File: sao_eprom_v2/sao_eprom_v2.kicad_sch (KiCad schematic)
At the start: 8 parts, among them J1 USB_C_Receptacle_USB2.0, J2 Conn_01x03, U1 RP2040, X1 YSO110TR

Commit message: More works on eprom v2
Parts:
- removed U?: 74LS161, symbol 74xx:74LS161
- removed U?: 27C512, Package_DIP:DIP-28_W15.24mm, symbol Memory_EPROM:27C512
- added C1, C2, C3, C4: 100n, Capacitor_SMD:C_0402_1005Metric, symbol Device:C_Small
- added J3: Conn_02x03_Odd_Even, Connector_PinHeader_2.54mm:PinHeader_2x03_P2.54mm_Vertical, symbol Connector_Generic:Conn_02x03_Odd_Even
- added R1, R2, R3, R4, R5: 10K, Resistor_SMD:R_0402_1005Metric_Pad0.72x0.64mm_HandSolder, symbol Device:R
- added R8, R9: 27R, Resistor_SMD:R_0402_1005Metric_Pad0.72x0.64mm_HandSolder, symbol Device:R
- added U1: W25Q128JVS, Package_SO:SOIC-8_5.23x5.23mm_P1.27mm, symbol Memory_Flash:W25Q128JVS
- added U3: 24LC00, Package_SO:SOIC-8_3.9x4.9mm_P1.27mm, symbol Memory_EEPROM:24LC00
- J2: renamed from J1; footprint (none) -> Connector_USB:USB_C_Receptacle_G-Switch_GT-USB-7010ASV
- R6: renamed from R1; footprint Resistor_THT:R_Axial_DIN0207_L6.3mm_D2.5mm_P10.16mm_Horizontal -> Resistor_SMD:R_0402_1005Metric_Pad0.72x0.64mm_HandSolder
- R7: renamed from R2; footprint Resistor_THT:R_Axial_DIN0207_L6.3mm_D2.5mm_P10.16mm_Horizontal -> Resistor_SMD:R_0402_1005Metric_Pad0.72x0.64mm_HandSolder
- renumbered J2 to J1, U1 to U2
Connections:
- net +3V3: now also C1.2, C2.2, C3.2, C4.2, J3.2 (Pin_2), U1.8 (VCC), U3.8 (VCC)
- net GND: now also C1.1, C2.1, C3.1, C4.1, J3.1 (Pin_1), R1.2, R2.2, R3.2, R4.2, R5.2, U1.4 (GND), U3.1 (A0), U3.2 (A1), U3.3 (A2), U3.4 (GND), U3.7 (WP)
- net USB_DM: now also R8.2; no longer J2.A7 (D-), J2.B7 (D-)
- net USB_DP: now also R9.2; no longer J2.A6 (D+), J2.B6 (D+)
- net SBU1: now reaches J2.A8 (SBU1)
- net SBU1: now also J2.B8 (SBU2)
- net EPROM and level shifters/D0: now reaches U2.11 (GPIO8)
- net EPROM and level shifters/D1: now reaches U2.12 (GPIO9)
- net EPROM and level shifters/D2: now reaches U2.13 (GPIO10)
- net EPROM and level shifters/D3: now reaches U2.14 (GPIO11)
- net EPROM and level shifters/D4: now reaches U2.15 (GPIO12)
- net EPROM and level shifters/D5: now reaches U2.16 (GPIO13)
- net EPROM and level shifters/D6: now reaches U2.17 (GPIO14)
- net EPROM and level shifters/D7: now reaches U2.18 (GPIO15)
- net EPROM and level shifters/A0: now reaches U2.2 (GPIO0)
- net EPROM and level shifters/OE: now reaches U2.27 (GPIO16)
- net EPROM and level shifters/~{OE}: now reaches U2.28 (GPIO17)
- net EPROM and level shifters/ALS: now reaches U2.29 (GPIO18)
- net EPROM and level shifters/A1: now reaches U2.3 (GPIO1)
- net EPROM and level shifters/AHS: now reaches U2.30 (GPIO19)
- net SDA: now reaches U2.31 (GPIO20)
- net SDA: now also J3.4 (Pin_4), U3.5 (SDA)
- net SCL: now reaches U2.32 (GPIO21)
- net SCL: now also J3.3 (Pin_3), U3.6 (SCL)
- net Power generation/5VEN: now reaches U2.34 (GPIO22)
- net Power generation/5VEN: now also R1.1
- net Power generation/12V75EN: now reaches U2.35 (GPIO23)
- net Power generation/12V75EN: now also R2.1
- net Power generation/VppAEN: now reaches U2.36 (GPIO24)
- net Power generation/VppAEN: now also R3.1
- net Power generation/VppBEN: now reaches U2.37 (GPIO25)
- net Power generation/VppBEN: now also R4.1
- net Power generation/VdetEN: now reaches U2.38 (GPIO26_ADC0)
- net Power generation/VdetEN: now also R5.1
- net EPROM and level shifters/A2: now reaches U2.4 (GPIO2)
- net EPROM and level shifters/A3: now reaches U2.5 (GPIO3)
- net at U2.51 (QSPI_SD3): now also U1.7 (IO3)
- net at U2.52 (QSPI_SCLK): now also U1.6 (CLK)
- net at U2.53 (QSPI_SD0): now also U1.5 (DI(IO0))
- net at U2.54 (QSPI_SD2): now also U1.3 (IO2)
- net at U2.55 (QSPI_SD1): now also U1.2 (DO(IO1))
- net at U2.56 (QSPI_SS): now also U1.1 (~{CS})
- net EPROM and level shifters/A4: now reaches U2.6 (GPIO4)
- net EPROM and level shifters/A5: now reaches U2.7 (GPIO5)
- net EPROM and level shifters/A6: now reaches U2.8 (GPIO6)
- net EPROM and level shifters/A7: now reaches U2.9 (GPIO7)
- new net: J2.A6 (D+), J2.B6 (D+), R9.1
- new net: J2.A7 (D-), J2.B7 (D-), R8.1
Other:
- added sheet EPROM and level shifters (eprom.kicad_sch)
- added sheet Power generation (power.kicad_sch)
- note added: "Logic level 3.3V"
- moved on the sheet: J1, J2, R6, R7, U2, X1

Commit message: the experiment
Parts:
- removed J3: Conn_02x03_Odd_Even, Connector_PinHeader_2.54mm:PinHeader_2x03_P2.54mm_Vertical, symbol Connector_Generic:Conn_02x03_Odd_Even
- added C14, C15, C16, C17, C18, C19, C20, C21, C22: 100n, Capacitor_SMD:C_0402_1005Metric_Pad0.74x0.62mm_HandSolder, symbol Device:C_Small
- added J3: sao_v2_addon_tht, simple_add_on_v2:sao_v2_addon_tht, symbol simple_add_on_v2:sao_v2_addon_tht
- C1, C2, C3, C4: footprint Capacitor_SMD:C_0402_1005Metric -> Capacitor_SMD:C_0402_1005Metric_Pad0.74x0.62mm_HandSolder
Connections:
- net +3V3: now also C14.1, C15.1, C16.2, C17.2, C18.2, C19.2, C20.2, J3.1 (3V3)
- net GND: now also C14.2, C15.2, C16.1, C17.1, C18.1, C19.1, C20.1, C21.1, C22.1, J3.2 (GND)
- net SBU1: now also U2.40 (GPIO28_ADC2); no longer J2.B8 (SBU2)
- net SCL: now also J3.4 (SCL)
- net SDA: now also J3.3 (SDA)
- net +1V1: now reaches U2.23 (DVDD), U2.45 (VREG_VOUT), U2.50 (DVDD)
- net +1V1: now also C21.2, C22.2
- net SBU2: now reaches U2.41 (GPIO29_ADC3)
- net SBU2: now also J2.B8 (SBU2)
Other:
- moved on the sheet: C1, C2, C3, C4

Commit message: More tricky routing.
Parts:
- added C23: 100n, Capacitor_SMD:C_0402_1005Metric_Pad0.74x0.62mm_HandSolder, symbol Device:C_Small
- added H1, H2, H3, H4: MountingHole_Pad, MountingHole:MountingHole_2.2mm_M2_Pad_Via, symbol Mechanical:MountingHole_Pad
- X1: value YSO110TR -> SX3M12.000M20F30TNN
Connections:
- net +3V3: now also C23.1
- net EPROM and level shifters/A0: now also U2.11 (GPIO8); no longer U2.2 (GPIO0)
- net EPROM and level shifters/A1: now also U2.12 (GPIO9); no longer U2.3 (GPIO1)
- net EPROM and level shifters/A2: now also U2.13 (GPIO10); no longer U2.4 (GPIO2)
- net EPROM and level shifters/A3: now also U2.14 (GPIO11); no longer U2.5 (GPIO3)
- net EPROM and level shifters/A4: now also U2.15 (GPIO12); no longer U2.6 (GPIO4)
- net EPROM and level shifters/A5: now also U2.16 (GPIO13); no longer U2.7 (GPIO5)
- net EPROM and level shifters/A6: now also U2.17 (GPIO14); no longer U2.8 (GPIO6)
- net EPROM and level shifters/A7: now also U2.18 (GPIO15); no longer U2.9 (GPIO7)
- net EPROM and level shifters/D0: now also U2.2 (GPIO0); no longer U2.11 (GPIO8)
- net EPROM and level shifters/D1: now also U2.3 (GPIO1); no longer U2.12 (GPIO9)
- net EPROM and level shifters/D2: now also U2.4 (GPIO2); no longer U2.13 (GPIO10)
- net EPROM and level shifters/D3: now also U2.5 (GPIO3); no longer U2.14 (GPIO11)
- net EPROM and level shifters/D4: now also U2.6 (GPIO4); no longer U2.15 (GPIO12)
- net EPROM and level shifters/D5: now also U2.7 (GPIO5); no longer U2.16 (GPIO13)
- net EPROM and level shifters/D6: now also U2.8 (GPIO6); no longer U2.17 (GPIO14)
- net EPROM and level shifters/D7: now also U2.9 (GPIO7); no longer U2.18 (GPIO15)
- net GND: now also C23.2, H1.1, H2.1, H3.1, H4.1
- net USB_D+: now reaches J2.A6 (D+), J2.B6 (D+), R9.1
- net USB_D-: now reaches J2.A7 (D-), J2.B7 (D-), R8.1
- net ~{QSPI_CS}: now reaches U1.1 (~{CS}), U2.56 (QSPI_SS)
- net QSPI_D1: now reaches U1.2 (DO(IO1)), U2.55 (QSPI_SD1)
- net QSPI_D2: now reaches U1.3 (IO2), U2.54 (QSPI_SD2)
- net QSPI_D0: now reaches U1.5 (DI(IO0)), U2.53 (QSPI_SD0)
- net QSPI_CLK: now reaches U1.6 (CLK), U2.52 (QSPI_SCLK)
- net QSPI_D3: now reaches U1.7 (IO3), U2.51 (QSPI_SD3)
- net USB_DM renamed RP2040_D-
- net USB_DP renamed RP2040_D+
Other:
- moved on the sheet: C15, R8, R9, U1

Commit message: Nearly finished the design
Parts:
- removed R1, R2: 10K, Resistor_SMD:R_0402_1005Metric_Pad0.72x0.64mm_HandSolder, symbol Device:R
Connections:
- net SWD_CLK: now reaches J1.3 (Pin_3), U2.24 (SWCLK)
- net SWD_DATA: now reaches J1.1 (Pin_1), U2.25 (SWD)
- net Power generation/12V75EN: no longer names the net of U2.35 (GPIO23)
- net Power generation/5VEN: no longer names the net of U2.34 (GPIO22)
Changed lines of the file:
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@@
   (junction (at 113.03 25.4) (diameter 0) (color 0 0 0 0)
   )
-  (junction (at 132.08 100.33) (diameter 0) (color 0 0 0 0)
-  )
   (junction (at 97.79 33.02) (diameter 0) (color 0 0 0 0)
   )
@@
   (junction (at 118.11 33.02) (diameter 0) (color 0 0 0 0)
   )
-  (junction (at 129.54 97.79) (diameter 0) (color 0 0 0 0)
-  )
   (junction (at 123.19 25.4) (diameter 0) (color 0 0 0 0)
   )
@@
   (junction (at 107.95 33.02) (diameter 0) (color 0 0 0 0)
   )
-  (junction (at 132.08 133.35) (diameter 0) (color 0 0 0 0)
-  )
   (junction (at 113.03 33.02) (diameter 0) (color 0 0 0 0)
   )
-  (junction (at 134.62 133.35) (diameter 0) (color 0 0 0 0)
-  )
   (junction (at 115.57 33.02) (diameter 0) (color 0 0 0 0)
   )
@@
     (stroke (width 0) (type default))
   )
-  (wire (pts (xy 132.08 100.33) (xy 152.4 100.33))
-    (stroke (width 0) (type default))
-  )
   (wire (pts (xy 139.7 110.49) (xy 128.27 110.49))
     (stroke (width 0) (type default))
@@
     (stroke (width 0) (type default))
   )
-  (wire (pts (xy 129.54 97.79) (xy 153.67 97.79))
-    (stroke (width 0) (type default))
-  )
   (wire (pts (xy 128.27 72.39) (xy 156.21 72.39))
     (stroke (width 0) (type default))
@@
     (stroke (width 0) (type default))
   )
-  (wire (pts (xy 132.08 100.33) (xy 132.08 120.65))
-    (stroke (width 0) (type default))
-  )
   (wire (pts (xy 128.27 44.45) (xy 156.21 44.45))
     (stroke (width 0) (type default))
@@
     (stroke (width 0) (type default))
   )
-  (wire (pts (xy 153.67 102.87) (xy 156.21 102.87))
-    (stroke (width 0) (type default))
-  )
   (wire (pts (xy 64.77 64.77) (xy 77.47 64.77))
     (stroke (width 0) (type default))
   )
-  (wire (pts (xy 153.67 97.79) (xy 153.67 102.87))
-    (stroke (width 0) (type default))
-  )
   (wire (pts (xy 139.7 133.35) (xy 137.16 133.35))
     (stroke (width 0) (type default))
@@
     (stroke (width 0) (type default))
   )
-  (wire (pts (xy 152.4 105.41) (xy 152.4 100.33))
-    (stroke (width 0) (type default))
-  )
   (wire (pts (xy 176.53 102.87) (xy 176.53 41.91))
     (stroke (width 0) (type default))
@@
     (stroke (width 0) (type default))
   )
-  (wire (pts (xy 128.27 97.79) (xy 129.54 97.79))
-    (stroke (width 0) (type default))
-  )
   (wire (pts (xy 123.19 33.02) (xy 125.73 33.02))
     (stroke (width 0) (type default))
@@
     (stroke (width 0) (type default))
   )
-  (wire (pts (xy 156.21 105.41) (xy 152.4 105.41))
-    (stroke (width 0) (type default))
-  )
   (wire (pts (xy 128.27 115.57) (xy 140.97 115.57))
     (stroke (width 0) (type default))
@@
     (stroke (width 0) (type default))
   )
-  (wire (pts (xy 132.08 133.35) (xy 134.62 133.35))
-    (stroke (width 0) (type default))
-  )
-  (wire (pts (xy 128.27 100.33) (xy 132.08 100.33))
-    (stroke (width 0) (type default))
-  )
   (wire (pts (xy 107.95 25.4) (xy 110.49 25.4))
     (stroke (width 0) (type default))
@@
     (stroke (width 0) (type default))
   )
-  (wire (pts (xy 129.54 133.35) (xy 132.08 133.35))
-    (stroke (width 0) (type default))
-  )
   (wire (pts (xy 128.27 54.61) (xy 156.21 54.61))
     (stroke (width 0) (type default))
@@
     (stroke (width 0) (type default))
   )
-  (wire (pts (xy 132.08 128.27) (xy 132.08 133.35))
-    (stroke (width 0) (type default))
-  )
   (wire (pts (xy 66.04 107.95) (xy 77.47 107.95))
     (stroke (width 0) (type default))
@@
     (stroke (width 0) (type default))
   )
-  (wire (pts (xy 129.54 128.27) (xy 129.54 133.35))
-    (stroke (width 0) (type default))
-  )
   (wire (pts (xy 74.93 62.23) (xy 74.93 74.93))
     (stroke (width 0) (type default))
@@
   )
   (wire (pts (xy 110.49 31.75) (xy 110.49 33.02))
-    (stroke (width 0) (type default))
-  )
-  (wire (pts (xy 129.54 97.79) (xy 129.54 120.65))
     (stroke (width 0) (type default))
   )
@@
     (effects (font (size 1.27 1.27)) (justify left bottom))
   )
+  (label "SWD_DATA" (at 68.58 113.03 0) (fields_autoplaced)
+    (effects (font (size 0.3 0.3)) (justify left bottom))
+  )
   (label "QSPI_D3" (at 64.77 72.39 0) (fields_autoplaced)
     (effects (font (size 1.27 1.27)) (justify left bottom))
+  )
+  (label "SWD_CLK" (at 68.58 107.95 0) (fields_autoplaced)
+    (effects (font (size 0.3 0.3)) (justify left bottom))
   )
   (label "QSPI_D1" (at 64.77 67.31 0) (fields_autoplaced)
@@
         (path "/07beccdd-32b3-4f03-aa51-fb5544b6f2d4"
           (reference "#PWR068") (unit 1)
+        )
+      )
+    )
+  )
+  (symbol (lib_id "power:+3V3") (at 156.21 102.87 90) (unit 1)
+    (in_bom yes) (on_board yes) (dnp no) (fields_autoplaced)
+    (property "Reference" "#PWR075" (at 160.02 102.87 0)
+      (effects (font (size 1.27 1.27)) hide)
+    )
+    (property "Value" "+3V3" (at 152.4 102.87 90)
+      (effects (font (size 1.27 1.27)) (justify left))
+    )
+    (property "Footprint" "" (at 156.21 102.87 0)
+      (effects (font (size 1.27 1.27)) hide)
+    )
+    (property "Datasheet" "" (at 156.21 102.87 0)
+      (effects (font (size 1.27 1.27)) hide)
+    )
+    (pin "1")
+    (instances
+      (project "sao_eprom_v2"
+        (path "/07beccdd-32b3-4f03-aa51-fb5544b6f2d4"
+          (reference "#PWR075") (unit 1)
         )
       )
@@
     )
   )
+  (symbol (lib_id "power:+3V3") (at 156.21 105.41 90) (unit 1)
+    (in_bom yes) (on_board yes) (dnp no) (fields_autoplaced)
+    (property "Reference" "#PWR076" (at 160.02 105.41 0)
+      (effects (font (size 1.27 1.27)) hide)
+    )
+    (property "Value" "+3V3" (at 152.4 105.41 90)
+      (effects (font (size 1.27 1.27)) (justify left))
+    )
+    (property "Footprint" "" (at 156.21 105.41 0)
+      (effects (font (size 1.27 1.27)) hide)
+    )
+    (property "Datasheet" "" (at 156.21 105.41 0)
+      (effects (font (size 1.27 1.27)) hide)
+    )
+    (pin "1")
+    (instances
+      (project "sao_eprom_v2"
+        (path "/07beccdd-32b3-4f03-aa51-fb5544b6f2d4"
+          (reference "#PWR076") (unit 1)
+        )
+      )
+    )
+  )
   (symbol (lib_id "Device:R") (at 71.12 52.07 90) (unit 1)
     (in_bom yes) (on_board yes) (dnp no)
@@
         (path "/07beccdd-32b3-4f03-aa51-fb5544b6f2d4"
           (reference "#PWR071") (unit 1)
-        )
-      )
-    )
-  )
-  (symbol (lib_id "Device:R") (at 129.54 124.46 0) (unit 1)
-    (in_bom yes) (on_board yes) (dnp no)
-    (property "Reference" "R1" (at 129.54 124.46 90)
-      (effects (font (size 1.27 1.27)))
-    )
-    (property "Value" "10K" (at 130.81 128.27 90)
-      (effects (font (size 1.27 1.27)) (justify right))
-    )
-    (property "Footprint" "Resistor_SMD:R_0402_1005Metric_Pad0.72x0.64mm_HandSolder" (at 127.762 124.46 90)
-      (effects (font (size 1.27 1.27)) hide)
-    )
-    (property "Datasheet" "~" (at 129.54 124.46 0)
-      (effects (font (size 1.27 1.27)) hide)
-    )
-    (pin "1")
-    (pin "2")
-    (instances
-      (project "sao_eprom_v2"
-        (path "/07beccdd-32b3-4f03-aa51-fb5544b6f2d4"
-          (reference "R1") (unit 1)
         )
       )
@@
         )
       )
-    )
-  )
-  (symbol (lib_id "Device:R") (at 132.08 124.46 0) (unit 1)
-    (in_bom yes) (on_board yes) (dnp no)
-    (property "Reference" "R2" (at 132.08 124.46 90)
-      (effects (font (size 1.27 1.27)))
-    )
-    (property "Value" "10K" (at 133.35 128.27 90)
-      (effects (font (size 1.27 1.27)) (justify right))
-    )
-    (property "Footprint" "Resistor_SMD:R_0402_1005Metric_Pad0.72x0.64mm_HandSolder" (at 130.302 124.46 90)
-      (effects (font (size 1.27 1.27)) hide)
-    )
-    (property "Datasheet" "~" (at 132.08 124.46 0)
-      (effects (font (size 1.27 1.27)) hide)
-    )
-    (pin "1")
-    (pin "2")
-    (instances
-      (project "sao_eprom_v2"
-        (path "/07beccdd-32b3-4f03-aa51-fb5544b6f2d4"
-          (reference "R2") (unit 1)
-        )
-      )

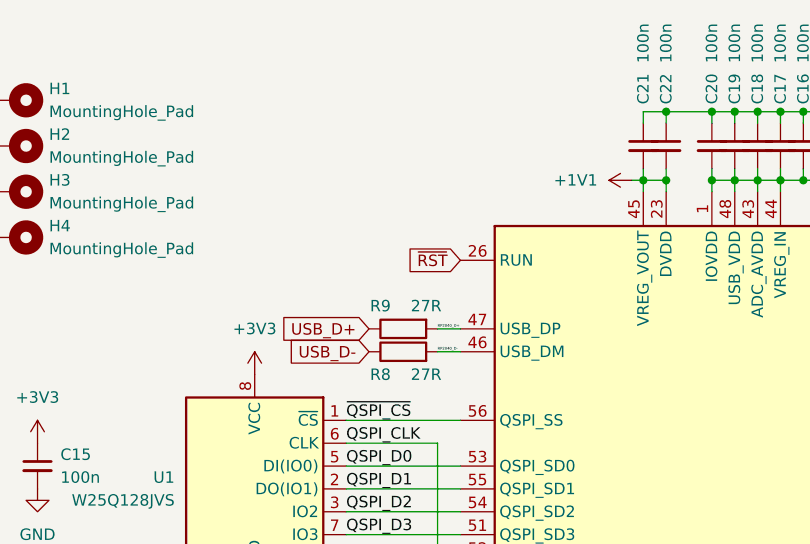
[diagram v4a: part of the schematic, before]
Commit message: First complete PCB
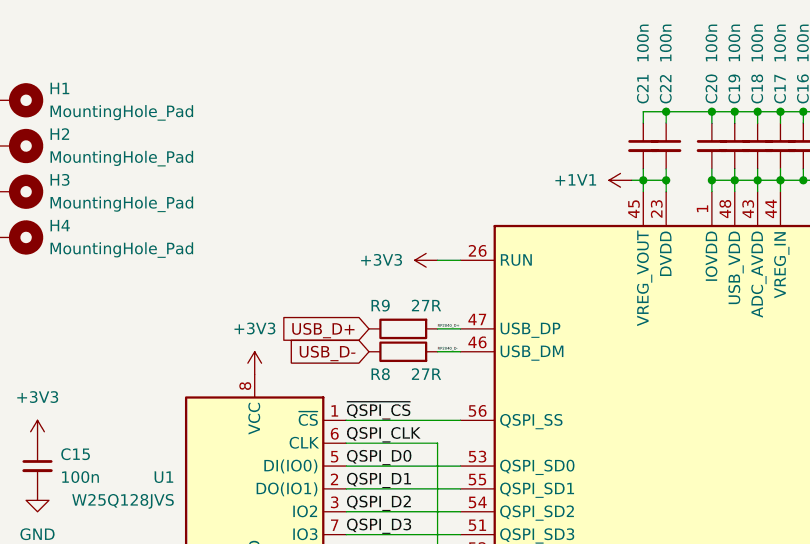
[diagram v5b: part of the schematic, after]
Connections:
- net ~{RST} is gone; now on net +3V3: U2.26 (RUN)
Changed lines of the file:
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@@
+    (stroke (width 0) (type default))
+  )
+  (wire (pts (xy 74.93 41.91) (xy 77.47 41.91))
     (stroke (width 0) (type default))
   )
@@
     (property "Intersheetrefs" "${INTERSHEET_REFS}" (at 53.6453 172.72 0)
       (effects (font (size 1.27 1.27)) (justify left) hide)
-    )
-  )
-  (global_label "~{RST}" (shape input) (at 77.47 41.91 180) (fields_autoplaced)
-    (effects (font (size 1.27 1.27)) (justify right))
-    (property "Intersheetrefs" "${INTERSHEET_REFS}" (at 71.6098 41.8306 0)
-      (effects (font (size 1.27 1.27)) (justify right) hide)
     )
   )
@@
         )
       )
+    )
+  )
+  (symbol (lib_id "power:+3V3") (at 74.93 41.91 90) (unit 1)
+    (in_bom yes) (on_board yes) (dnp no) (fields_autoplaced)
+    (property "Reference" "#PWR077" (at 78.74 41.91 0)
+      (effects (font (size 1.27 1.27)) hide)
+    )
+    (property "Value" "+3V3" (at 71.12 41.91 90)
+      (effects (font (size 1.27 1.27)) (justify left))
+    )
+    (property "Footprint" "" (at 74.93 41.91 0)
+      (effects (font (size 1.27 1.27)) hide)
+    )
+    (property "Datasheet" "" (at 74.93 41.91 0)
+      (effects (font (size 1.27 1.27)) hide)
+    )
+    (pin "1")
+    (instances
+      (project "sao_eprom_v2"
+        (path "/07beccdd-32b3-4f03-aa51-fb5544b6f2d4"
+          (reference "#PWR077") (unit 1)
+        )
+      )
